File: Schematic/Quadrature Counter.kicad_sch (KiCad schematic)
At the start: 8 parts, among them U20 LS7366R-S, U21 LS7366R-S, Y1 ASV-30.000MHZ-E-T

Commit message: 100n cap
100n cap bom
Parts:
- C73: footprint (none) -> CL10B104MB8NNNC:CAPC1608X90N; Link (none) -> https://mou.sr/3JWJm45; Manufacturer Part Number (none) -> CL10B104MB8NNNC; Price per Unit (none) -> 0.10; Supplier (none) -> Mouser; Supplier Part Number (none) -> 187-CL10B104MB8NNNC
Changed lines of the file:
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@@
 			)
 		)
-		(property "Footprint" ""
+		(property "Footprint" "CL10B104MB8NNNC:CAPC1608X90N"
 			(at 67.6148 97.79 0)
 			(effects
@@
 			)
 		)
-		(property "Link" ""
-			(at 68.58 101.6 0)
-			(effects
-				(font
-					(size 1.27 1.27)
-				)
-				(hide yes)
-			)
-		)
-		(property "Manufacturer Part Number" ""
-			(at 68.58 101.6 0)
-			(effects
-				(font
-					(size 1.27 1.27)
-				)
-				(hide yes)
-			)
-		)
-		(property "Price per Unit" ""
-			(at 68.58 101.6 0)
-			(effects
-				(font
-					(size 1.27 1.27)
-				)
-				(hide yes)
-			)
-		)
-		(property "Supplier" ""
-			(at 68.58 101.6 0)
-			(effects
-				(font
-					(size 1.27 1.27)
-				)
-				(hide yes)
-			)
-		)
-		(property "Supplier Part Number" ""
-			(at 68.58 101.6 0)
-			(effects
+		(property "Link" "https://mou.sr/3JWJm45"
+			(at 68.58 101.6 0)
+			(effects
+				(font
+					(size 1.27 1.27)
+				)
+				(hide yes)
+			)
+		)
+		(property "Manufacturer Part Number" "CL10B104MB8NNNC"
+			(at 68.58 101.6 0)
+			(effects
+				(font
+					(size 1.27 1.27)
+				)
+				(hide yes)
+			)
+		)
+		(property "Price per Unit" "0.10"
+			(at 68.58 101.6 0)
+			(effects
+				(font
+					(size 1.27 1.27)
+				)
+				(hide yes)
+			)
+		)
+		(property "Supplier" "Mouser"
+			(at 68.58 101.6 0)
+			(effects
+				(font
+					(size 1.27 1.27)
+				)
+				(hide yes)
+			)
+		)
+		(property "Supplier Part Number" "187-CL10B104MB8NNNC "
+			(at 68.58 101.6 0)
+			(effects

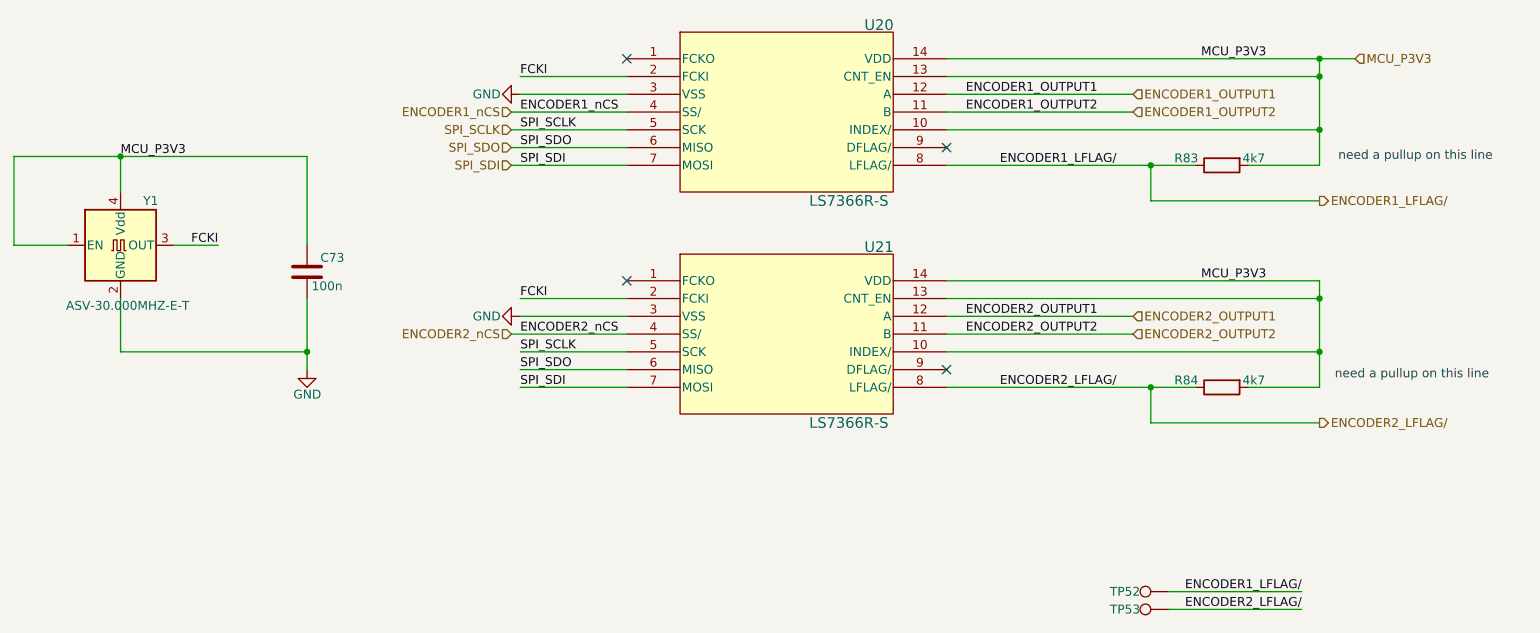
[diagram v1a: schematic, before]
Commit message: added test points and fet
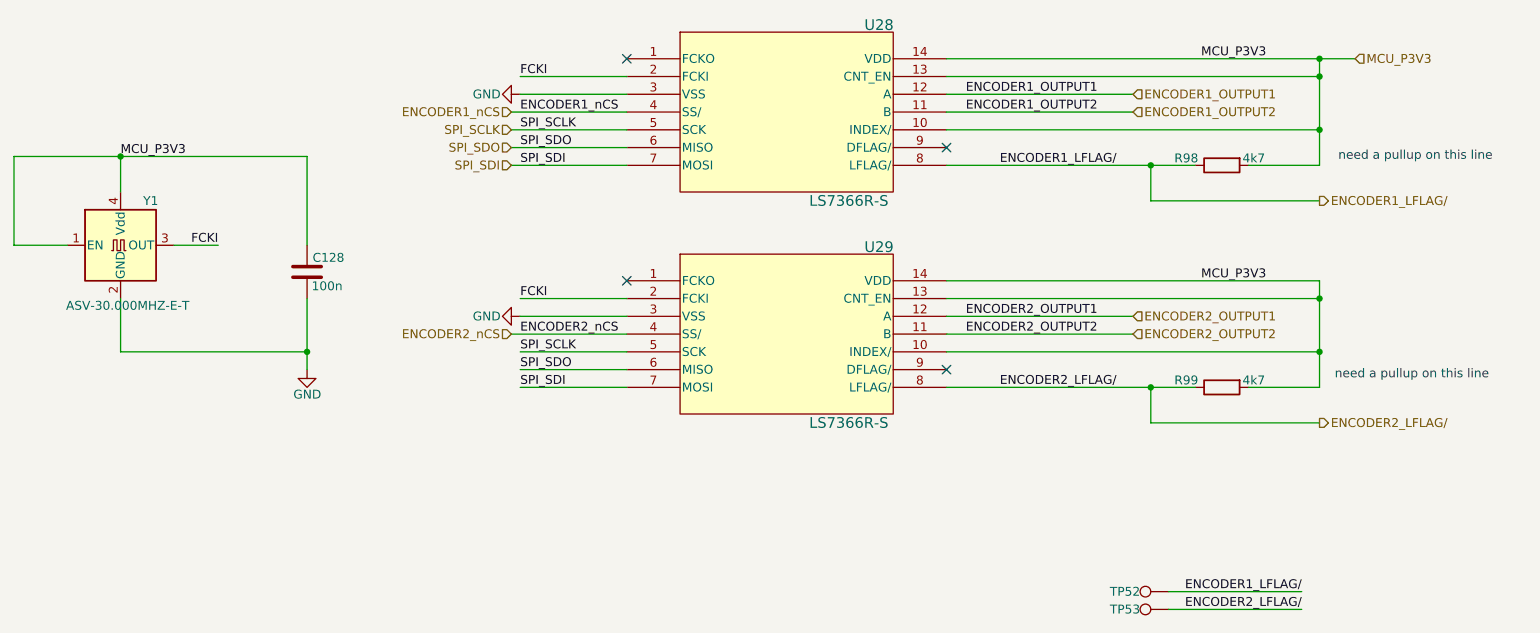
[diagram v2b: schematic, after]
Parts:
- C128: renamed from C73; footprint CL10B104MB8NNNC:CAPC1608X90N -> Capacitor_SMD:C_0603_1608Metric_Pad1.08x0.95mm_HandSolder
- TP52, TP53: footprint (none) -> 5017:5017; Link (none) -> https://mou.sr/4gj83nj; Manufacturer Part Number (none) -> 5017; Price per Unit (none) -> 0.21; Supplier (none) -> Mouser; Supplier Part Number (none) -> 534-5017
- renumbered R83 to R98, R84 to R99, U20 to U28, U21 to U29
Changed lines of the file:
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@@
 		(on_board yes)
 		(dnp no)
-		(property "Reference" "U20"
+		(property "Reference" "U28"
 			(at 150.368 66.294 0)
 			(effects
@@
 			(project "STAR"
 				(path "/fc8533bc-25dd-4c20-9b4c-ffebebd6739b/f73d6367-f3ba-42df-a3ea-bd155f1c219f/12bd6774-3c71-41d8-bbdc-bae46e746955"
-					(reference "U20")
+					(reference "U28")
 					(unit 1)
 				)
@@
 		(on_board yes)
 		(dnp no)
-		(property "Reference" "#PWR052"
+		(property "Reference" "#PWR077"
 			(at 92.71 107.95 0)
 			(effects
@@
 			(project "STAR"
 				(path "/fc8533bc-25dd-4c20-9b4c-ffebebd6739b/f73d6367-f3ba-42df-a3ea-bd155f1c219f/12bd6774-3c71-41d8-bbdc-bae46e746955"
-					(reference "#PWR052")
+					(reference "#PWR077")
 					(unit 1)
 				)
@@
 		(on_board yes)
 		(dnp no)
-		(property "Reference" "R83"
+		(property "Reference" "R98"
 			(at 194.31 85.344 90)
 			(effects
@@
 			(project "STAR"
 				(path "/fc8533bc-25dd-4c20-9b4c-ffebebd6739b/f73d6367-f3ba-42df-a3ea-bd155f1c219f/12bd6774-3c71-41d8-bbdc-bae46e746955"
-					(reference "R83")
+					(reference "R98")
 					(unit 1)
 				)
@@
 		(on_board yes)
 		(dnp no)
-		(property "Reference" "C73"
+		(property "Reference" "C128"
 			(at 73.914 99.568 0)
 			(effects
@@
 			)
 		)
-		(property "Footprint" "CL10B104MB8NNNC:CAPC1608X90N"
+		(property "Footprint" "Capacitor_SMD:C_0603_1608Metric_Pad1.08x0.95mm_HandSolder"
 			(at 67.6148 97.79 0)
 			(effects
@@
 			(project "STAR"
 				(path "/fc8533bc-25dd-4c20-9b4c-ffebebd6739b/f73d6367-f3ba-42df-a3ea-bd155f1c219f/12bd6774-3c71-41d8-bbdc-bae46e746955"
-					(reference "C73")
+					(reference "C128")
 					(unit 1)
 				)
@@
 			)
 		)
-		(property "Footprint" ""
+		(property "Footprint" "5017:5017"
 			(at 191.77 142.24 0)
 			(effects
@@
 			)
 		)
-		(property "Link" ""
+		(property "Link" "https://mou.sr/4gj83nj"
 			(at 191.77 147.32 90)
 			(effects
@@
 			)
 		)
-		(property "Manufacturer Part Number" ""
+		(property "Manufacturer Part Number" "5017"
 			(at 191.77 147.32 90)
 			(effects
@@
 			)
 		)
-		(property "Price per Unit" ""
+		(property "Price per Unit" "0.21"
 			(at 191.77 147.32 90)
 			(effects
@@
 			)
 		)
+		(property "Supplier" "Mouser"
+			(at 191.77 147.32 90)
+			(effects
+				(font
+					(size 1.27 1.27)
+				)
+				(hide yes)
+			)
+		)
+		(property "Supplier Part Number" "534-5017"
+			(at 191.77 147.32 90)
+			(effects
+				(font
+					(size 1.27 1.27)
+				)
+				(hide yes)
+			)
+		)
 		(pin "1"
 		)
@@
 		(on_board yes)
 		(dnp no)
-		(property "Reference" "U21"
+		(property "Reference" "U29"
 			(at 150.368 98.044 0)
 			(effects
@@
 			(project "STAR"
 				(path "/fc8533bc-25dd-4c20-9b4c-ffebebd6739b/f73d6367-f3ba-42df-a3ea-bd155f1c219f/12bd6774-3c71-41d8-bbdc-bae46e746955"
-					(reference "U21")
+					(reference "U29")
 					(unit 1)
 				)
@@
 		(on_board yes)
 		(dnp no)
-		(property "Reference" "#PWR050"
+		(property "Reference" "#PWR075"
 			(at 68.58 121.92 0)
 			(effects
@@
 			(project "STAR"
 				(path "/fc8533bc-25dd-4c20-9b4c-ffebebd6739b/f73d6367-f3ba-42df-a3ea-bd155f1c219f/12bd6774-3c71-41d8-bbdc-bae46e746955"
-					(reference "#PWR050")
+					(reference "#PWR075")
 					(unit 1)
 				)
@@
 		(on_board yes)
 		(dnp no)
-		(property "Reference" "R84"
+		(property "Reference" "R99"
 			(at 194.31 117.094 90)
 			(effects
@@
 			(project "STAR"
 				(path "/fc8533bc-25dd-4c20-9b4c-ffebebd6739b/f73d6367-f3ba-42df-a3ea-bd155f1c219f/12bd6774-3c71-41d8-bbdc-bae46e746955"
-					(reference "R84")
+					(reference "R99")
 					(unit 1)
 				)
@@
 		(on_board yes)
 		(dnp no)
-		(property "Reference" "#PWR051"
+		(property "Reference" "#PWR076"
 			(at 92.71 76.2 0)
 			(effects
@@
 			(project "STAR"
 				(path "/fc8533bc-25dd-4c20-9b4c-ffebebd6739b/f73d6367-f3ba-42df-a3ea-bd155f1c219f/12bd6774-3c71-41d8-bbdc-bae46e746955"
-					(reference "#PWR051")
+					(reference "#PWR076")
 					(unit 1)
 				)
@@
 			)
 		)
-		(property "Footprint" ""
+		(property "Footprint" "5017:5017"
 			(at 191.77 144.78 0)
 			(effects
@@
 			)
 		)
-		(property "Link" ""
+		(property "Link" "https://mou.sr/4gj83nj"
 			(at 191.77 149.86 90)
 			(effects
@@
 			)
 		)
-		(property "Manufacturer Part Number" ""
+		(property "Manufacturer Part Number" "5017"
 			(at 191.77 149.86 90)
 			(effects
@@
 			)
 		)
-		(property "Price per Unit" ""
+		(property "Price per Unit" "0.21"
 			(at 191.77 149.86 90)
 			(effects
@@
 			(at 191.77 149.86 90)
 			(effects
+				(font
+					(size 1.27 1.27)
+				)
+				(hide yes)
+			)
+		)
+		(property "Supplier" "Mouser"
+			(at 191.77 149.86 90)
+			(effects
+				(font
+					(size 1.27 1.27)
+				)
+				(hide yes)
+			)
+		)
+		(property "Supplier Part Number" "534-5017"
+			(at 191.77 149.86 90)
+			(effects

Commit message: usb-c
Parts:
- TP52, TP53: footprint 5017:5017 -> 3825:3825; Link https://mou.sr/4gj83nj -> https://mou.sr/3MgWhw3; Manufacturer Part Number 5017 -> 3825; Price per Unit 0.21 -> 9.95; Supplier Part Number 534-5017 -> 485-3825
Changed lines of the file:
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@@
 			)
 		)
-		(property "Footprint" "5017:5017"
+		(property "Footprint" "3825:3825"
 			(at 191.77 142.24 0)
 			(effects
@@
 			)
 		)
-		(property "Link" "https://mou.sr/4gj83nj"
-			(at 191.77 147.32 90)
-			(effects
-				(font
-					(size 1.27 1.27)
-				)
-				(hide yes)
-			)
-		)
-		(property "Manufacturer Part Number" "5017"
-			(at 191.77 147.32 90)
-			(effects
-				(font
-					(size 1.27 1.27)
-				)
-				(hide yes)
-			)
-		)
-		(property "Price per Unit" "0.21"
+		(property "Link" "https://mou.sr/3MgWhw3"
+			(at 191.77 147.32 90)
+			(effects
+				(font
+					(size 1.27 1.27)
+				)
+				(hide yes)
+			)
+		)
+		(property "Manufacturer Part Number" "3825"
+			(at 191.77 147.32 90)
+			(effects
+				(font
+					(size 1.27 1.27)
+				)
+				(hide yes)
+			)
+		)
+		(property "Price per Unit" "9.95"
 			(at 191.77 147.32 90)
 			(effects
@@
 			)
 		)
-		(property "Supplier Part Number" "534-5017"
+		(property "Supplier Part Number" "485-3825"
 			(at 191.77 147.32 90)
 			(effects
@@
 			)
 		)
-		(property "Footprint" "5017:5017"
+		(property "Footprint" "3825:3825"
 			(at 191.77 144.78 0)
 			(effects
@@
 			)
 		)
-		(property "Link" "https://mou.sr/4gj83nj"
-			(at 191.77 149.86 90)
-			(effects
-				(font
-					(size 1.27 1.27)
-				)
-				(hide yes)
-			)
-		)
-		(property "Manufacturer Part Number" "5017"
-			(at 191.77 149.86 90)
-			(effects
-				(font
-					(size 1.27 1.27)
-				)
-				(hide yes)
-			)
-		)
-		(property "Price per Unit" "0.21"
+		(property "Link" "https://mou.sr/3MgWhw3"
+			(at 191.77 149.86 90)
+			(effects
+				(font
+					(size 1.27 1.27)
+				)
+				(hide yes)
+			)
+		)
+		(property "Manufacturer Part Number" "3825"
+			(at 191.77 149.86 90)
+			(effects
+				(font
+					(size 1.27 1.27)
+				)
+				(hide yes)
+			)
+		)
+		(property "Price per Unit" "9.95"
 			(at 191.77 149.86 90)
 			(effects
@@
 			)
 		)
-		(property "Supplier Part Number" "534-5017"
-			(at 191.77 149.86 90)
-			(effects
+		(property "Supplier Part Number" "485-3825"
+			(at 191.77 149.86 90)
+			(effects

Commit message: More REsistor
16 res down for bom
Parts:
- R98, R99: footprint (none) -> Resistor_SMD:R_0603_1608Metric_Pad0.98x0.95mm_HandSolder; Link (none) -> https://mou.sr/48a41vp; Manufacturer Part Number (none) -> RCS06034K70FKEA; Price per Unit (none) -> 0.13; Supplier (none) -> Mouser; Supplier Part Number (none) -> 71-RCS06034K70FKEA
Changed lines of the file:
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@@
 			)
 		)
-		(property "Footprint" ""
+		(property "Footprint" "Resistor_SMD:R_0603_1608Metric_Pad0.98x0.95mm_HandSolder"
 			(at 199.39 84.582 90)
 			(effects
@@
 			)
 		)
-		(property "Link" ""
-			(at 199.39 86.36 90)
-			(effects
-				(font
-					(size 1.27 1.27)
-				)
-				(hide yes)
-			)
-		)
-		(property "Manufacturer Part Number" ""
-			(at 199.39 86.36 90)
-			(effects
-				(font
-					(size 1.27 1.27)
-				)
-				(hide yes)
-			)
-		)
-		(property "Price per Unit" ""
+		(property "Link" "https://mou.sr/48a41vp"
+			(at 199.39 86.36 90)
+			(effects
+				(font
+					(size 1.27 1.27)
+				)
+				(hide yes)
+			)
+		)
+		(property "Manufacturer Part Number" "RCS06034K70FKEA "
+			(at 199.39 86.36 90)
+			(effects
+				(font
+					(size 1.27 1.27)
+				)
+				(hide yes)
+			)
+		)
+		(property "Price per Unit" "0.13"
 			(at 199.39 86.36 90)
 			(effects
@@
 		)
 		(property "Specifications" ""
+			(at 199.39 86.36 90)
+			(effects
+				(font
+					(size 1.27 1.27)
+				)
+				(hide yes)
+			)
+		)
+		(property "Supplier" "Mouser"
+			(at 199.39 86.36 90)
+			(effects
+				(font
+					(size 1.27 1.27)
+				)
+				(hide yes)
+			)
+		)
+		(property "Supplier Part Number" "71-RCS06034K70FKEA "
 			(at 199.39 86.36 90)
 			(effects
@@
 			)
 		)
-		(property "Footprint" ""
+		(property "Footprint" "Resistor_SMD:R_0603_1608Metric_Pad0.98x0.95mm_HandSolder"
 			(at 199.39 116.332 90)
 			(effects
@@
 			)
 		)
-		(property "Link" ""
-			(at 199.39 118.11 90)
-			(effects
-				(font
-					(size 1.27 1.27)
-				)
-				(hide yes)
-			)
-		)
-		(property "Manufacturer Part Number" ""
-			(at 199.39 118.11 90)
-			(effects
-				(font
-					(size 1.27 1.27)
-				)
-				(hide yes)
-			)
-		)
-		(property "Price per Unit" ""
+		(property "Link" "https://mou.sr/48a41vp"
+			(at 199.39 118.11 90)
+			(effects
+				(font
+					(size 1.27 1.27)
+				)
+				(hide yes)
+			)
+		)
+		(property "Manufacturer Part Number" "RCS06034K70FKEA "
+			(at 199.39 118.11 90)
+			(effects
+				(font
+					(size 1.27 1.27)
+				)
+				(hide yes)
+			)
+		)
+		(property "Price per Unit" "0.13"
 			(at 199.39 118.11 90)
 			(effects
@@
 			(at 199.39 118.11 90)
 			(effects
+				(font
+					(size 1.27 1.27)
+				)
+				(hide yes)
+			)
+		)
+		(property "Supplier" "Mouser"
+			(at 199.39 118.11 90)
+			(effects
+				(font
+					(size 1.27 1.27)
+				)
+				(hide yes)
+			)
+		)
+		(property "Supplier Part Number" "71-RCS06034K70FKEA "
+			(at 199.39 118.11 90)
+			(effects

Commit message: Added DigiKey to BOM
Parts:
- C128: DigiKey Link (none) -> https://www.digikey.com/short/2nhzzz3n; DigiKey Part Number (none) -> CL10B104MB8NNNC; DigiKey Price per Unit (none) -> 0.08; Link https://mou.sr/3JWJm45 -> (none); Manufactaurer Part Number (none) -> CL10B104MB8NNNC; Manufacturer Part Number CL10B104MB8NNNC -> (none); Mouser Link (none) -> https://mou.sr/3JWJm45; Mouser Part Number (none) -> 187-CL10B104MB8NNNC; Mouser Price per Unit (none) -> 0.10; Price per Unit 0.10 -> (none); Supplier Mouser -> (none); Supplier Part Number 187-CL10B104MB8NNNC -> (none)
- R98, R99: DigiKey Link (none) -> https://www.digikey.com/short/0wt4qm7j; DigiKey Part Number (none) -> 541-2792-2-ND; DigiKey Price per Unit (none) -> 0.13; Link https://mou.sr/48a41vp -> (none); Manufactaurer Part Number (none) -> RCS06034K70FKEA; Manufacturer Part Number RCS06034K70FKEA -> (none); Mouser Link (none) -> https://mou.sr/48a41vp; Mouser Part Number (none) -> 71-RCS06034K70FKEA; Mouser Price per Unit (none) -> 0.13; Price per Unit 0.13 -> (none); Supplier Mouser -> (none); Supplier Part Number 71-RCS06034K70FKEA -> (none)
- TP52, TP53: DigiKey Link (none) -> https://www.digikey.com/short/n04bqb2d; DigiKey Part Number (none) -> 1528-3825-ND; DigiKey Price per Unit (none) -> 9.95; Link https://mou.sr/3MgWhw3 -> (none); Manufactaurer Part Number (none) -> 3825; Manufacturer Part Number 3825 -> (none); Mouser Link (none) -> https://mou.sr/3MgWhw3; Mouser Part Number (none) -> 485-3825; Mouser Price per Unit (none) -> 9.95; Price per Unit 9.95 -> (none); Supplier Mouser -> (none); Supplier Part Number 485-3825 -> (none)
- U28, U29: DigiKey Link (none) -> https://www.digikey.com/short/q4p5z99m; DigiKey Part Number (none) -> 2808-LS7366R-S-ND; DigiKey Price per Unit (none) -> 6.32; Manufactaurer Part Number (none) -> LS7366R-S; Mouser Link (none) -> N/A; Mouser Part Number (none) -> N/A; Mouser Price per Unit (none) -> N/A
- Y1: DigiKey Link (none) -> https://www.digikey.com/short/fmdj4bm0; DigiKey Part Number (none) -> 535-9319-2-ND; DigiKey Price per Unit (none) -> 1.30; Manufactaurer Part Number (none) -> ASV-25.000MHZ-EJ-T; Mouser Link (none) -> https://mou.sr/4n13zEv; Mouser Part Number (none) -> 815-ASV-25-EJ-T; Mouser Price per Unit (none) -> 1.24

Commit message: need to do Qs now
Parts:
- C128: DigiKey Part Number CL10B104MB8NNNC -> (none)
- R98, R99: DigiKey Part Number 541-2792-2-ND -> (none)
- TP49: renamed from TP52; DigiKey Part Number 1528-3825-ND -> (none)
- TP50: renamed from TP53; DigiKey Part Number 1528-3825-ND -> (none)
- U26: renamed from U28; DigiKey Part Number 2808-LS7366R-S-ND -> (none)
- U27: renamed from U29; DigiKey Part Number 2808-LS7366R-S-ND -> (none)
- Y1: DigiKey Part Number 535-9319-2-ND -> (none)
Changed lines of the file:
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@@
 		(on_board yes)
 		(dnp no)
-		(property "Reference" "U28"
+		(property "Reference" "U26"
 			(at 150.368 66.294 0)
 			(effects
@@
 			)
 		)
-		(property "DigiKey Part Number" "2808-LS7366R-S-ND"
+		(property "DigiKey Part Number" ""
 			(at 114.3 71.12 0)
 			(effects
@@
 			(project "STAR"
 				(path "/fc8533bc-25dd-4c20-9b4c-ffebebd6739b/f73d6367-f3ba-42df-a3ea-bd155f1c219f/12bd6774-3c71-41d8-bbdc-bae46e746955"
-					(reference "U28")
+					(reference "U26")
 					(unit 1)
 				)
@@
 			)
 		)
-		(property "DigiKey Part Number" "535-9319-2-ND "
+		(property "DigiKey Part Number" ""
 			(at 41.91 97.79 0)
 			(effects
@@
 			)
 		)
-		(property "DigiKey Part Number" "541-2792-2-ND"
+		(property "DigiKey Part Number" ""
 			(at 199.39 86.36 90)
 			(effects
@@
 			)
 		)
-		(property "DigiKey Part Number" "CL10B104MB8NNNC"
+		(property "DigiKey Part Number" ""
 			(at 68.58 101.6 0)
 			(effects
@@
 		(on_board yes)
 		(dnp no)
-		(property "Reference" "TP52"
+		(property "Reference" "TP49"
 			(at 187.706 147.32 90)
 			(effects
@@
 			)
 		)
-		(property "DigiKey Part Number" "1528-3825-ND"
+		(property "DigiKey Part Number" ""
 			(at 191.77 147.32 90)
 			(effects
@@
 			(project "STAR"
 				(path "/fc8533bc-25dd-4c20-9b4c-ffebebd6739b/f73d6367-f3ba-42df-a3ea-bd155f1c219f/12bd6774-3c71-41d8-bbdc-bae46e746955"
-					(reference "TP52")
+					(reference "TP49")
 					(unit 1)
 				)
@@
 		(on_board yes)
 		(dnp no)
-		(property "Reference" "U29"
+		(property "Reference" "U27"
 			(at 150.368 98.044 0)
 			(effects
@@
 			)
 		)
-		(property "DigiKey Part Number" "2808-LS7366R-S-ND"
+		(property "DigiKey Part Number" ""
 			(at 114.3 102.87 0)
 			(effects
@@
 			(project "STAR"
 				(path "/fc8533bc-25dd-4c20-9b4c-ffebebd6739b/f73d6367-f3ba-42df-a3ea-bd155f1c219f/12bd6774-3c71-41d8-bbdc-bae46e746955"
-					(reference "U29")
+					(reference "U27")
 					(unit 1)
 				)
@@
 			)
 		)
-		(property "DigiKey Part Number" "541-2792-2-ND"
+		(property "DigiKey Part Number" ""
 			(at 199.39 118.11 90)
 			(effects
@@
 		(on_board yes)
 		(dnp no)
-		(property "Reference" "TP53"
+		(property "Reference" "TP50"
 			(at 187.706 149.86 90)
 			(effects
@@
 			)
 		)
-		(property "DigiKey Part Number" "1528-3825-ND"
+		(property "DigiKey Part Number" ""
 			(at 191.77 149.86 90)
 			(effects
@@
 			(project "STAR"
 				(path "/fc8533bc-25dd-4c20-9b4c-ffebebd6739b/f73d6367-f3ba-42df-a3ea-bd155f1c219f/12bd6774-3c71-41d8-bbdc-bae46e746955"
-					(reference "TP53")
+					(reference "TP50")
 					(unit 1)
 				)
